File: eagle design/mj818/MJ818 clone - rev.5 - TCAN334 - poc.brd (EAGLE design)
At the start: 35 x 35 mm, 37 parts, among them IC202 LDK320AM33R, IC302 STM32F042G6U6, IC401 TCAN334, IC506 MAX16820, IC507 SQA470EEJ-T1_GE3, IC601 MAX16839, J101 Power Supply, J102 LED, J103 CAN

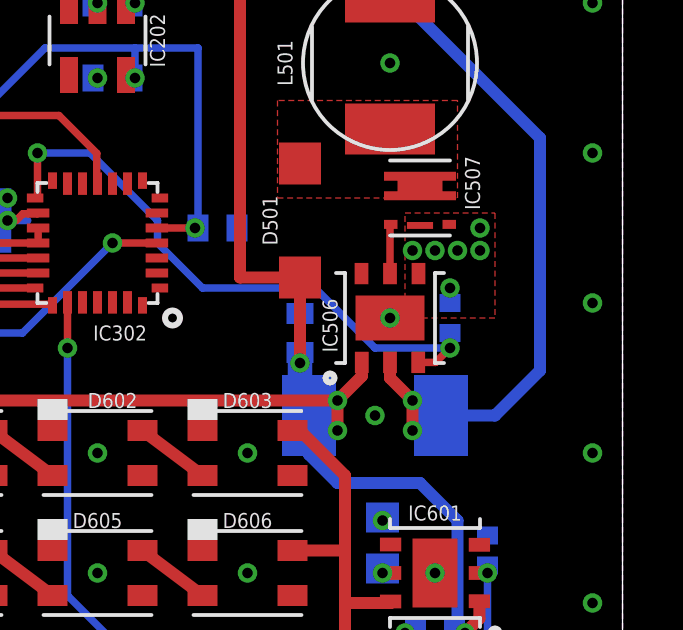
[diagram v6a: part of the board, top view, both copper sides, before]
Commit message: - validated that pulldown for MAX16820 dim line is not needed on MJ808/818
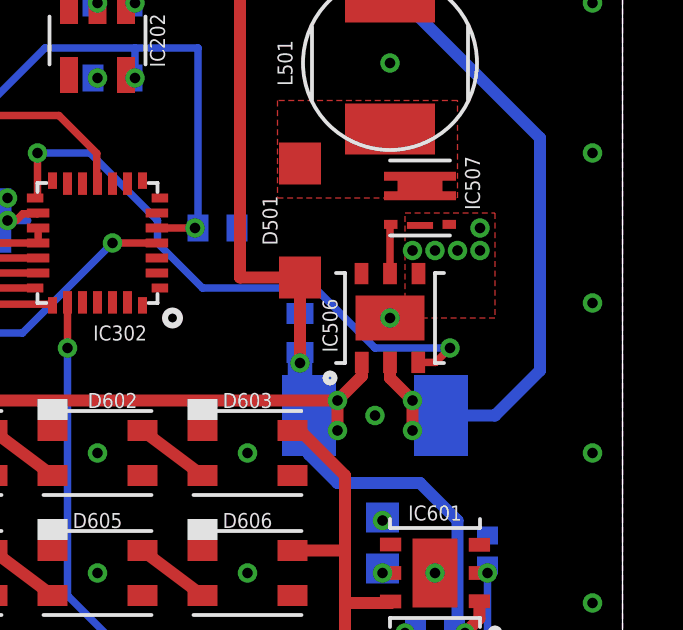
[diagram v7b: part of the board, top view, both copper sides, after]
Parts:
- removed R101: 10k, rcl:R0402
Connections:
- net DIM_BRAKE: no longer R101.2
- net GND: no longer R101.1
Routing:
- net DIM_BRAKE: track 20.2 -> 19.7 mm
- net GND: vias 51 -> 50
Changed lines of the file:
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@@
 <attribute name="VALUE" x="27.25" y="25.5" size="1" layer="27" font="vector" rot="R90" align="center"/>
-</element>
-<element name="R101" library="rcl" library_urn="urn:adsk.eagle:library:334" package="R0402" package3d_urn="urn:adsk.eagle:package:23547/3" value="10k" x="29.25" y="17" smashed="yes" rot="MR270">
-<attribute name="NAME" x="30.25" y="17" size="0.5" layer="26" font="fixed" rot="MR270" align="center"/>
-<attribute name="POPULARITY" value="0" x="29.25" y="17" size="1.778" layer="28" rot="MR270" display="off"/>
-<attribute name="SPICEPREFIX" value="R" x="29.25" y="17" size="1.778" layer="28" rot="MR270" display="off"/>
-<attribute name="VALUE" x="29.25" y="17" size="1.27" layer="28" rot="MR270"/>
 </element>
 <element name="R405" library="rcl" library_urn="urn:adsk.eagle:library:334" package="R0805" package3d_urn="urn:adsk.eagle:package:23553/2" value="60" x="10.16" y="26.924" smashed="yes" rot="MR270">
@@
 <signal name="GND">
 <contactref element="SWD101" pad="5_GND"/>
-<contactref element="R101" pad="1"/>
 <contactref element="C202" pad="2"/>
 <contactref element="C207" pad="1"/>
@@
 <via x="27.75" y="6.5" extent="1-16" drill="0.35"/>
 <via x="27.25" y="17" extent="1-16" drill="0.35"/>
-<via x="29.25" y="18" extent="1-16" drill="0.35"/>
 <via x="28" y="19.25" extent="1-16" drill="0.35"/>
 <via x="28.75" y="19.25" extent="1-16" drill="0.35"/>
@@
 </signal>
 <signal name="DIM_BRAKE" class="3">
-<contactref element="R101" pad="2"/>
 <contactref element="IC302" pad="15_PB1"/>
 <contactref element="IC506" pad="DIM"/>
@@
 <wire x1="28.19" y1="15.52" x2="28.77" y2="15.52" width="0.25" layer="1"/>
 <wire x1="28.77" y1="15.52" x2="29.25" y2="16" width="0.25" layer="1"/>
-<wire x1="29.25" y1="16" x2="29.25" y2="16.5" width="0.25" layer="16"/>
 <wire x1="26.75" y1="16" x2="29.25" y2="16" width="0.25" layer="16"/>
 <wire x1="26.75" y1="16" x2="24.75" y2="18" width="0.25" layer="16"/>

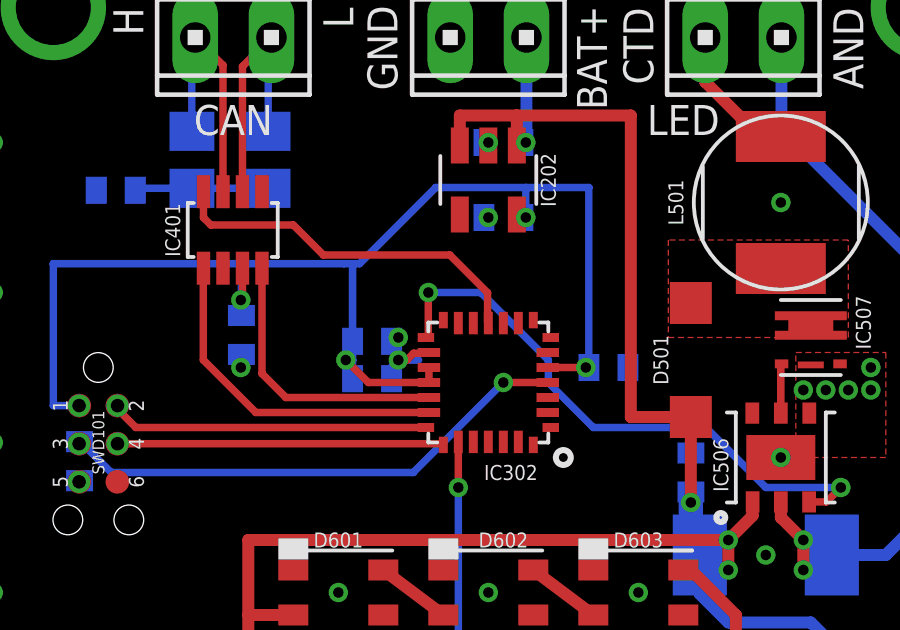
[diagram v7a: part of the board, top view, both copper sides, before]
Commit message: mj808/mj818: - moved pins off port B into port A
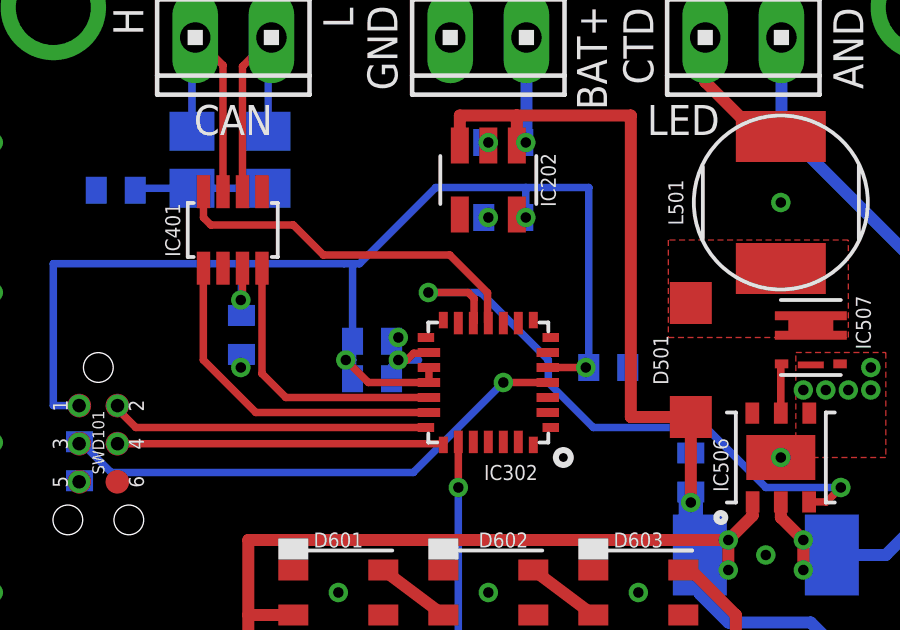
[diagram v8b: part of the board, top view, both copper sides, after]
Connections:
- net DIM_BRAKE: now also IC302.12_PA6; no longer IC302.15_PB1
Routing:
- net DIM_BRAKE: track 19.7 -> 20.6 mm
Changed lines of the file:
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@@
 </signal>
 <signal name="DIM_BRAKE" class="3">
-<contactref element="IC302" pad="15_PB1"/>
 <contactref element="IC506" pad="DIM"/>
 <via x="29.25" y="16" extent="1-16" drill="0.35"/>
 <via x="15.5" y="22.5" extent="1-16" drill="0.35"/>
-<wire x1="15.5" y1="22.5" x2="15.5" y2="21.08" width="0.25" layer="1"/>
-<wire x1="15.42" y1="21" x2="15.5" y2="21.08" width="0.25" layer="1"/>
 <wire x1="28.19" y1="15.52" x2="28.77" y2="15.52" width="0.25" layer="1"/>
 <wire x1="28.77" y1="15.52" x2="29.25" y2="16" width="0.25" layer="1"/>
@@
 <wire x1="21" y1="18" x2="19.5" y2="19.5" width="0.25" layer="16"/>
 <wire x1="24.75" y1="18" x2="21" y2="18" width="0.25" layer="16"/>
+<contactref element="IC302" pad="12_PA6"/>
+<wire x1="15.5" y1="22.5" x2="16.82821875" y2="22.5" width="0.25" layer="1"/>
+<wire x1="16.82821875" y1="22.5" x2="17.025" y2="22.30321875" width="0.25" layer="1"/>
+<wire x1="17.025" y1="22.30321875" x2="17.025" y2="21.505" width="0.25" layer="1"/>
+<wire x1="17.025" y1="21.505" x2="17" y2="21.48" width="0.25" layer="1"/>
 </signal>
 <signal name="DIM_REAR" class="3">
